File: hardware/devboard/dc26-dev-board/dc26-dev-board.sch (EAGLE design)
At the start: 3 parts, among them IC1 STM32F411RET6, U1 ESP-WROOM-32, Y1 ABL-8.000MHZ-B2

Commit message: WIP for board
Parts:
- added 3.3V-REGULATOR: BU33SD5WG-TR, dc-26:BU33SD5WG-TR
- added C1: 4.7uF, dc-26:C-USC1210
- added C2: 4.7uf, dc-26:C-USC1210
- added C3, C4: 1uf, dc-26:C-USC1206
- added CN1: (no value), dc-26:JST_2PIN-SMT-RA
- added IC10, IC11, IC12, IC13, IC14, IC15, IC16, IC2, IC3, IC4, IC5, IC6, IC7, IC8, IC9: APA104, APA104:APA104
- added LED1: MF-LED-0603-GREEN, dc-26:LED1206
- added R2: 470, dc-26:RESISTOR0805-RES
- added R3: 2k, dc-26:RESISTOR0805-RES
- added RESETTABLE-FUSE: SSSS811101, dc-26:PTCSMD
- added U$1: ST7735S_LCD_MODULE, dc-26:ST7735S_LCD_MODULE
- added U$2: DX4R005JJ2DX4R005JJ2, dc-26:DX4R005JJ2DX4R005JJ2
- added U$3: MCP73831, dc-26:DS21984E
- added U$4: STLINK-V2-CONNECTOR, dc-26:STLINK-V2-CONNECTOR
- added U$5: SWITCH_SPDT, dc-26:SWITCH_SPDT
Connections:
- new net GND: 3.3V-REGULATOR.GND, C1.2, C2.2, C3.1, C4.2, CN1.1, IC10.VSS, IC11.VSS, IC12.VSS, IC13.VSS, IC14.VSS, IC15.VSS, IC16.VSS, IC2.VSS, IC3.VSS, IC4.VSS, IC5.VSS, IC6.VSS, IC7.VSS, IC8.VSS, IC9.VSS, R3.1, U$2.GND, U$3.VSS, U$4.GND
- new net N$1: LED1.A, R2.1
- new net N$10: IC10.DOUT, IC14.DIN
- new net N$11: IC14.DOUT, IC7.DIN
- new net N$12: IC13.DIN, IC7.DOUT
- new net N$13: IC13.DOUT, IC6.DIN
- new net N$14: IC12.DIN, IC6.DOUT
- new net N$15: IC12.DOUT, IC5.DIN
- new net N$16: IC4.DIN, IC5.DOUT
- new net N$17: IC11.DIN, IC4.DOUT
- new net N$18: IC11.DOUT, IC3.DIN
- new net N$19: IC2.DIN, IC3.DOUT
- new net N$2: R3.2, U$3.PROG
- new net N$3: LED1.C, U$3.STAT
- new net N$4: 3.3V-REGULATOR.VIN, C3.2, RESETTABLE-FUSE.2, U$5.1
- new net N$5: IC15.DOUT, IC8.DIN
- new net N$6: 3.3V-REGULATOR.STBY, U$5.C
- new net N$7: IC8.DOUT, IC9.DIN
- new net N$8: IC16.DIN, IC9.DOUT
- new net N$9: IC10.DIN, IC16.DOUT
- new net SYS_JTCK_SWCLK: IC1.PA14, U$4.SWDCLK
- new net SYS_JTMS_SWDIO: IC1.PA13, U$4.SWDIO
- new net USB_DM: IC1.PA11, U$2.D+
- new net USB_DP: IC1.PA12, U$2.D-
- new net VCC: 3.3V-REGULATOR.VOUT, C4.1
- new net VCC0: C2.1, R2.2, U$2.+5V, U$3.VDD, U$4.VCC
- new net VCC1: C1.1, CN1.2, IC10.VDD, IC11.VDD, IC12.VDD, IC13.VDD, IC14.VDD, IC15.VDD, IC16.VDD, IC2.VDD, IC3.VDD, IC4.VDD, IC5.VDD, IC6.VDD, IC7.VDD, IC8.VDD, IC9.VDD, RESETTABLE-FUSE.1, U$3.VBAT
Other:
- note added: "APA104's need at least 3.5V"
- note added: "Battery JST 2 PIN"
- note added: "Battery, USB, ST-LINK Power Out"
- note added: "Input from USB / ST-LINK"
- note added: "power dissipation: Power Rule: P = I × V"
- moved on the sheet: IC1, U1, Y1

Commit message: power scheme done?
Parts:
- added C10, C11, C5, C6, C7, C9: 100nF, dc-26:C-USC1206
- added C12: 1uF, dc-26:C-USC1206
- added C8: 4.7uF, dc-26:C-USC1206
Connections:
- new net VBAT: IC1.VBAT
- new net VDD1: IC1.VDD(1)
- new net VDD2: IC1.VDD(2)
- new net VDD3: IC1.VDD(3)
- new net VDD4: IC1.VDD(4)
- new net VDDA: IC1.VDDA/VREF+
- new net VSS1: C6.2, IC1.VSS(1)
- new net VSS2: C7.2, IC1.VSS(2)
- new net VSS3: C5.2, IC1.VSS(3)
- new net VSS4: C9.2, IC1.VSS(4)
- new net VSSA: C11.2, C12.2, IC1.VSSA/VREF-
- net GND: now also C10.2, C8.2
- net VCC: now also C10.1, C11.1, C12.1, C5.1, C6.1, C7.1, C8.1, C9.1
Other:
- note added: "The VDD pins must be connected to VDD with external decoupling capacitors: one single Tantalum or Ceramic capacitor (min. 4.7 μF typ.10 μF) for the package + one 100 nF Ceramic capacitor for each VDD pin. • The VBAT pin can be connected to the external battery (1.65 V < VBAT < 3.6 V). If no external battery is used, it is recommended to connect this pin to VDD with a 100 nF external ceramic decou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"

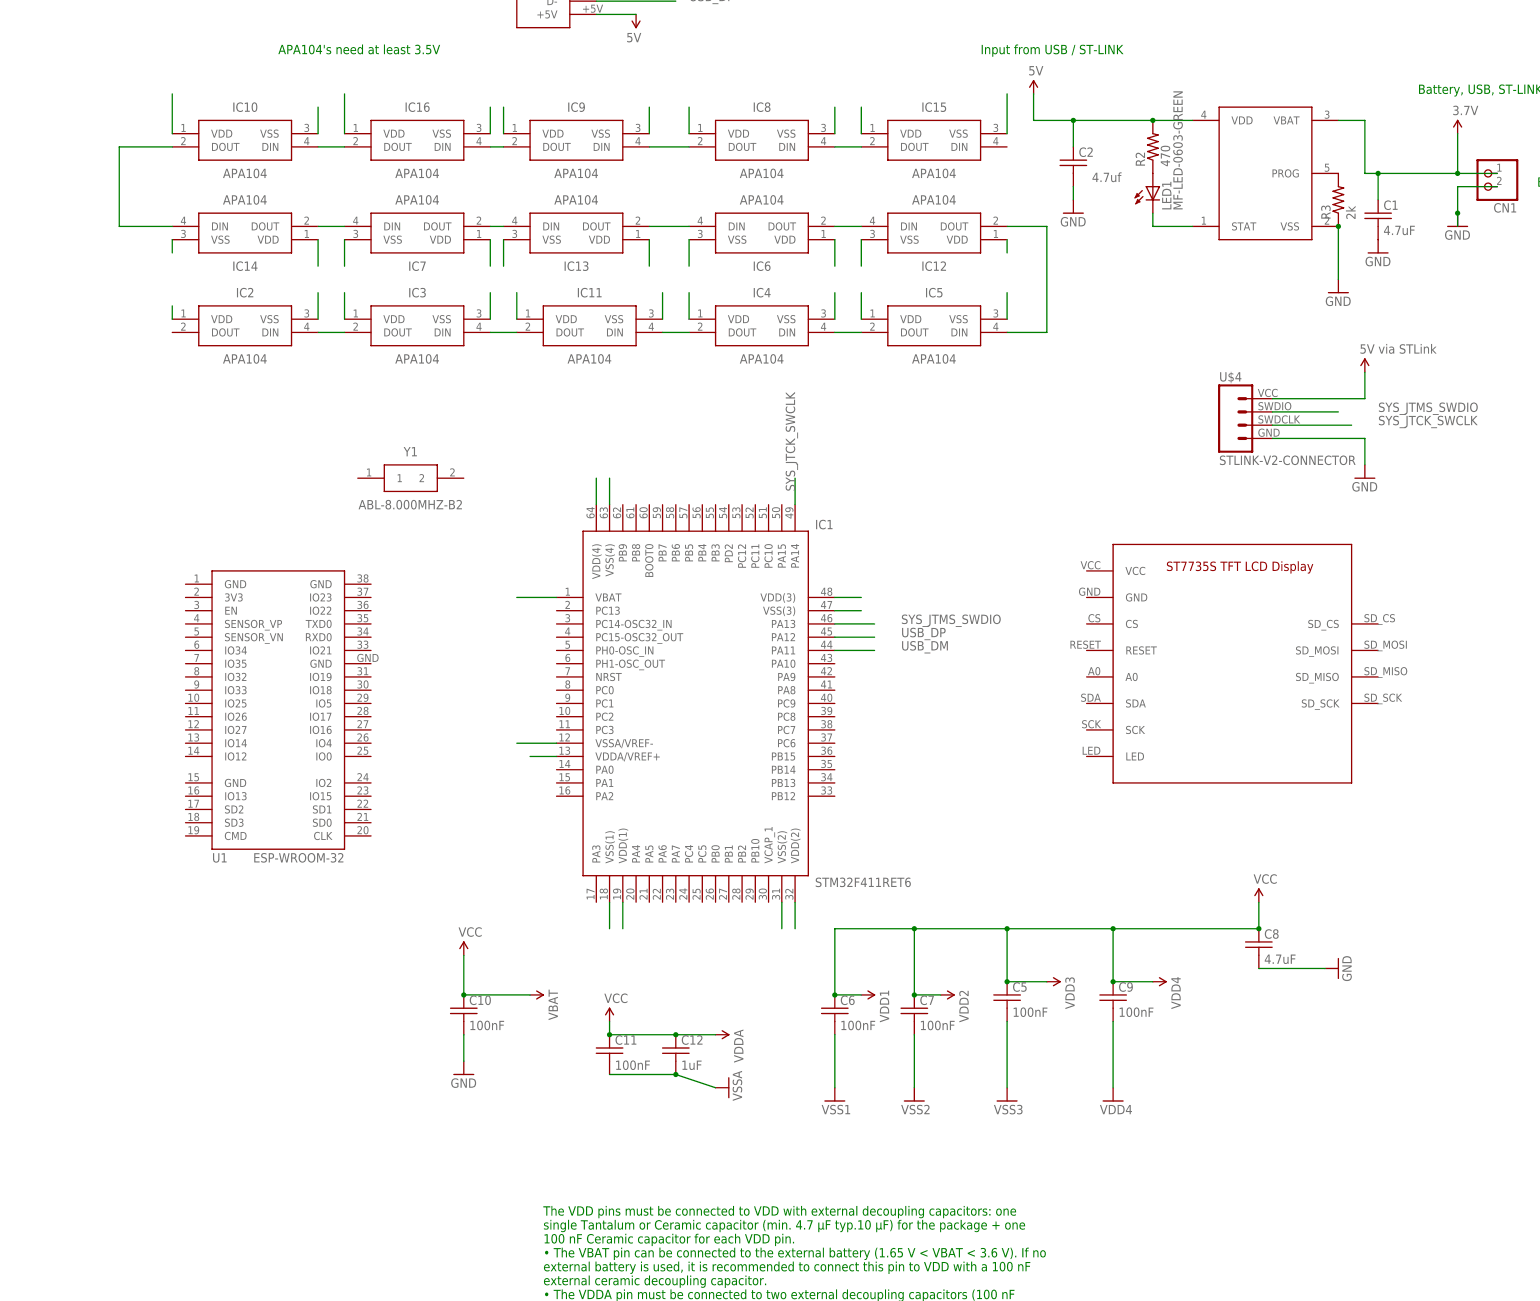
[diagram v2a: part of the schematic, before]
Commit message: more docs, added GPIOs for SD_CS and APA104s scemea farther along
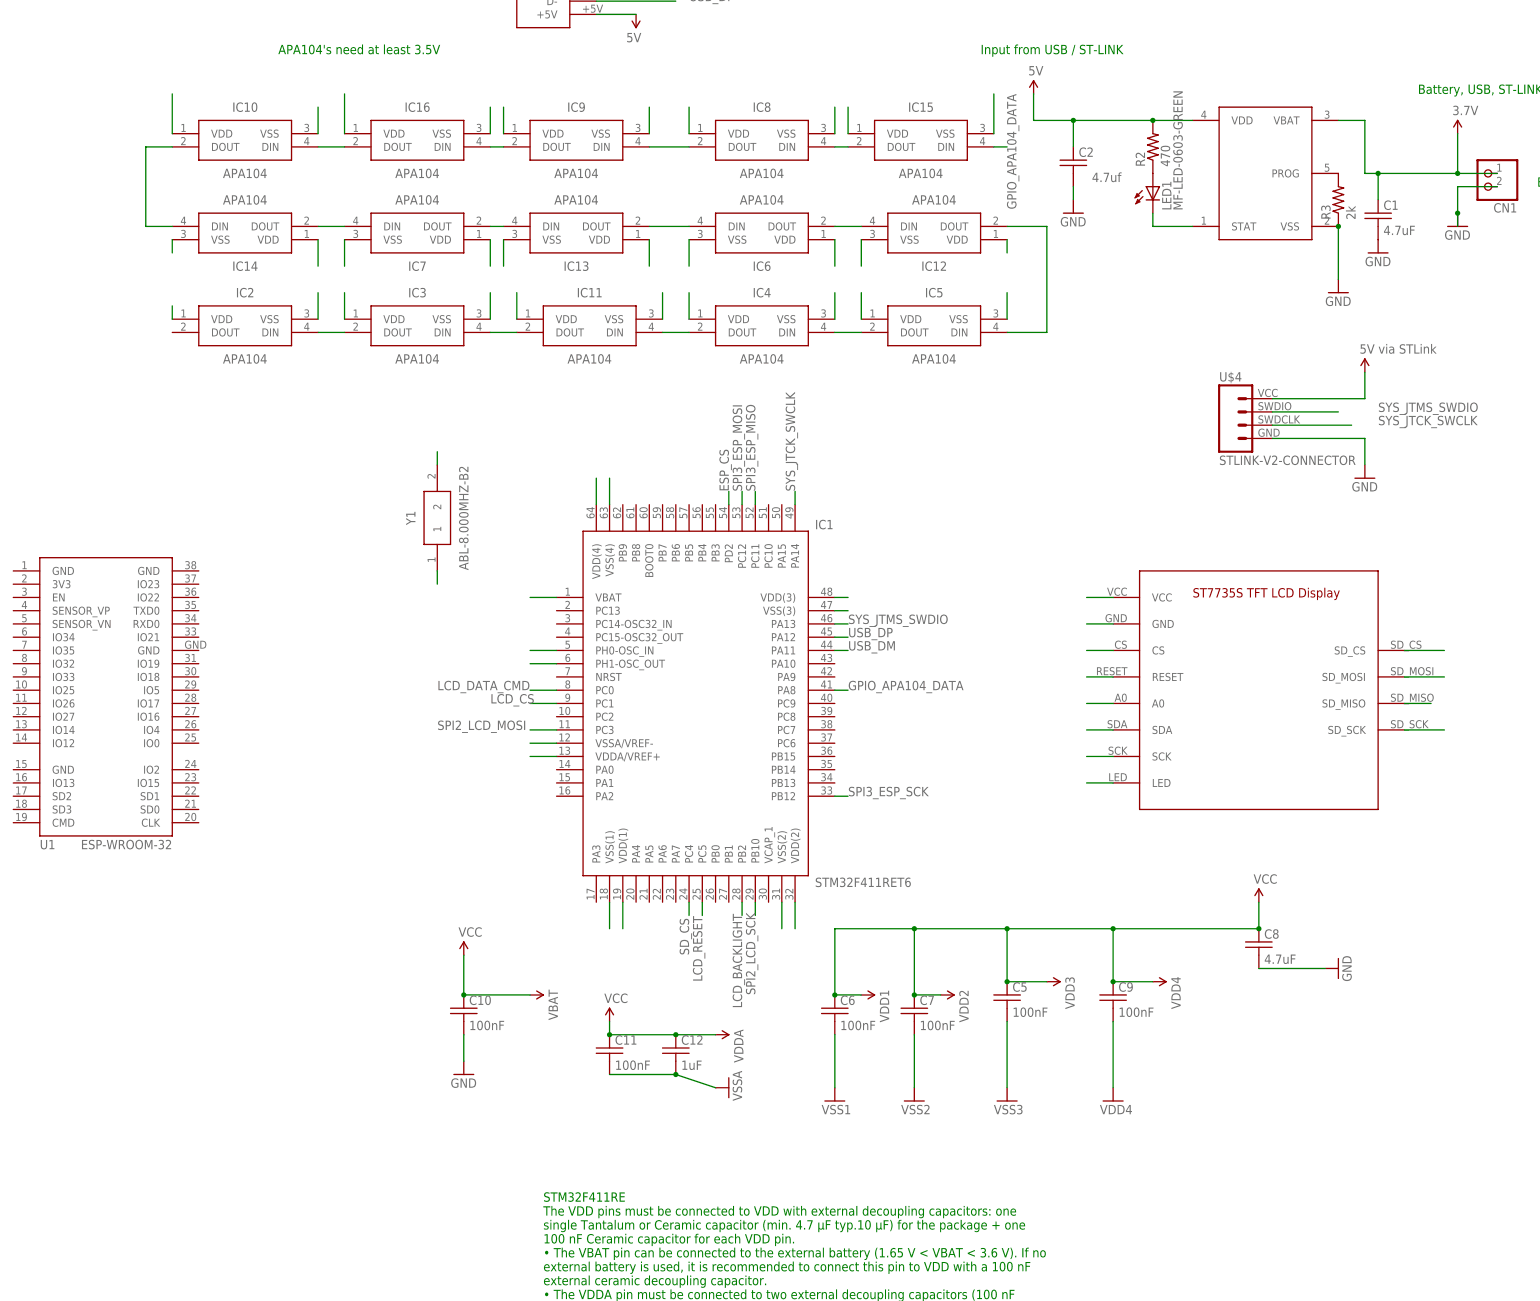
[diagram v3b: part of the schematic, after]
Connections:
- new net ESP_CS: IC1.PD2
- new net GPIO_APA104_DATA: IC1.PA8, IC15.DIN
- new net LCD_BACKLIGHT: IC1.PB2, U$1.LED
- new net LCD_CS: IC1.PC1, U$1.CS
- new net LCD_DATA_CMD: IC1.PC0, U$1.A0
- new net LCD_RESET: IC1.PC5, U$1.RESET
- new net OSC_IN: IC1.PH0-OSC_IN, Y1.2
- new net OSC_OUT: IC1.PH1-OSC_OUT, Y1.1
- new net SD_CS: IC1.PC4, U$1.SD_CS
- new net SPI2_LCD_MOSI: IC1.PC3, U$1.SDA
- new net SPI2_LCD_SCK: IC1.PB10, U$1.SCK
- new net SPI3_ESP_MISO: IC1.PC11, U$1.SD_MISO
- new net SPI3_ESP_MOSI: IC1.PC12, U$1.SD_MOSI
- new net SPI3_ESP_SCK: IC1.PB12, U$1.SD_SCK
- net GND: now also U$1.GND
- net VCC: now also U$1.VCC
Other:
- note added: "STM32F411RE The VDD pins must be connected to VDD with external decoupling capacitors: one single Tantalum or Ceramic capacitor (min. 4.7 μF typ.10 μF) for the package + one 100 nF Ceramic capacitor for each VDD pin. • The VBAT pin can be connected to the external battery (1.65 V < VBAT < 3.6 V). If no external battery is used, it is recommended to connect this pin to VDD with a 100 nF external c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"
- note removed: "The VDD pins must be connected to VDD with external decoupling capacitors: one single Tantalum or Ceramic capacitor (min. 4.7 μF typ.10 μF) for the package + one 100 nF Ceramic capacitor for each VDD pin. • The VBAT pin can be connected to the external battery (1.65 V < VBAT < 3.6 V). If no external battery is used, it is recommended to connect this pin to VDD with a 100 nF external ceramic decou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"
- moved on the sheet: IC15, U1, Y1
